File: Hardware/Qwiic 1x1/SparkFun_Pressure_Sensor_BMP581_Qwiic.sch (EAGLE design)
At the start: 25 parts, among them J1 QWIIC_RIGHT_ANGLE, J2 QWIIC_RIGHT_ANGLE, U1 BMP581

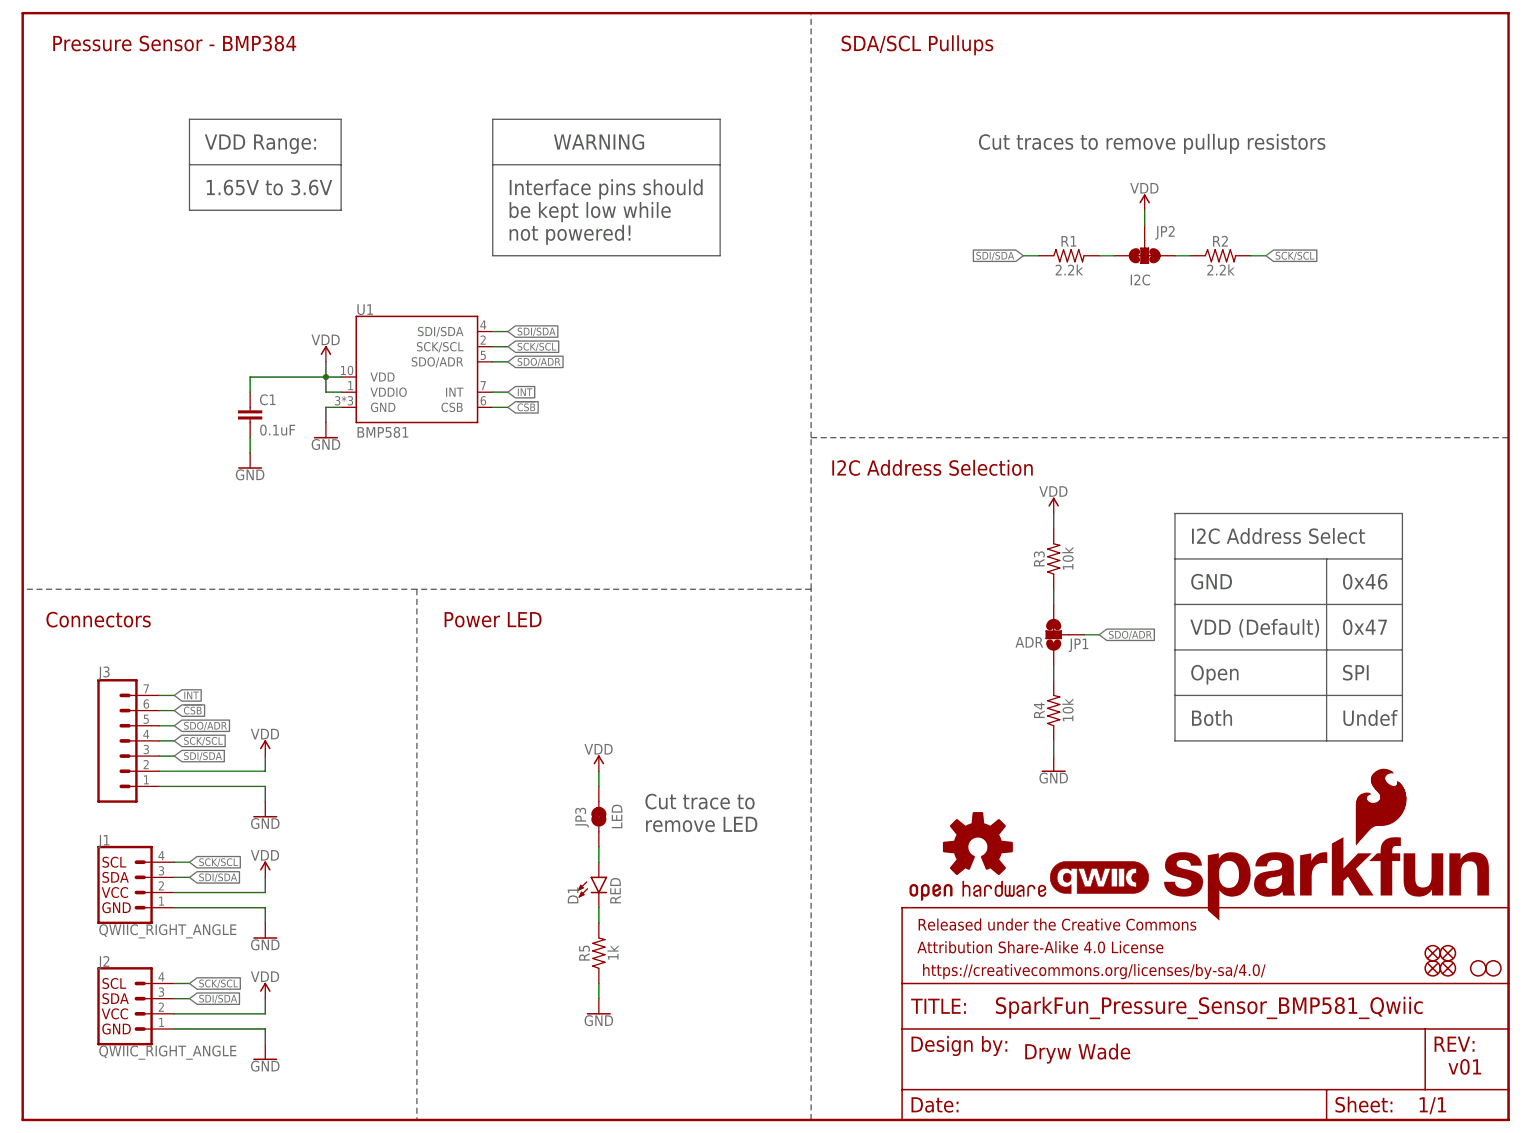
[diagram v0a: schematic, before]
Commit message: Design review updates
Rename files
Change to v10 (accelerating to reds)
Fix sensor name in schematic
Add note to schematic about max wire diameter in Micro PTH connectors
Update VDD range
Fix acid trap in Micro
Move PWR LED to give space
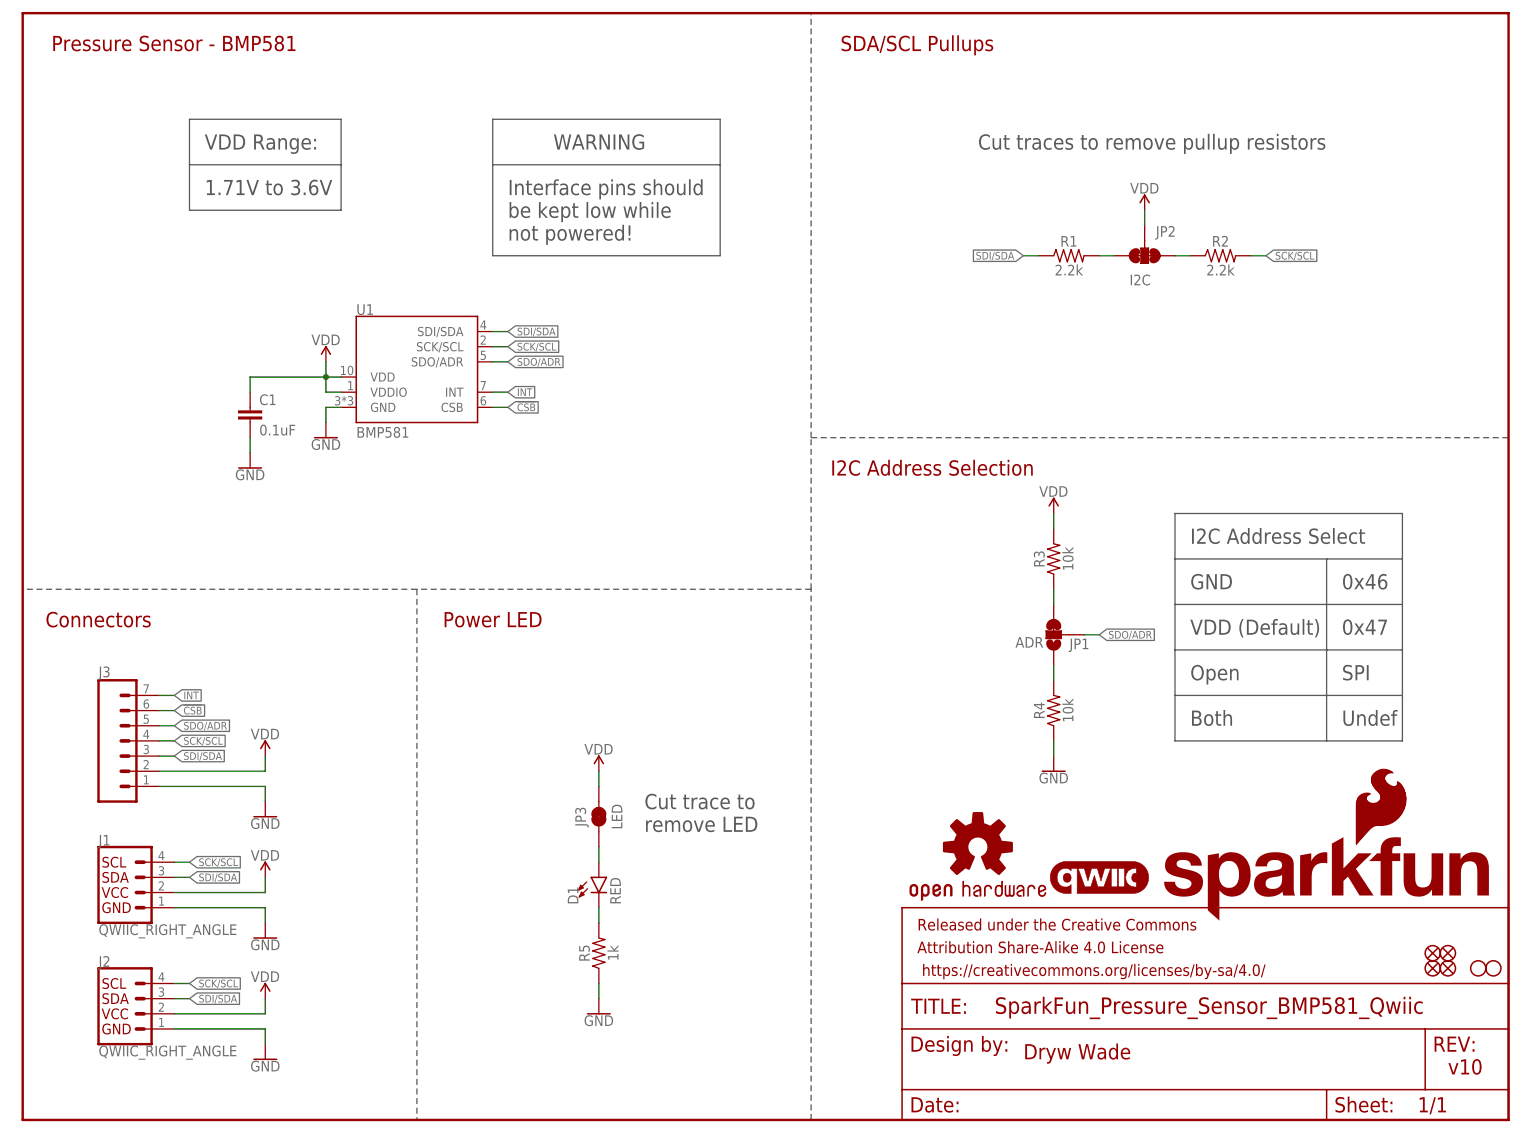
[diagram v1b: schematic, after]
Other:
- note added: "1.71V to 3.6V"
- note added: "Pressure Sensor - BMP581"
- note added: "v10"
- note removed: "1.65V to 3.6V"
- note removed: "Pressure Sensor - BMP384"
- note removed: "v01"
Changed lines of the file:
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@@
 <plain>
 <text x="167.64" y="10.16" size="2.54" layer="94" font="vector">Dryw Wade</text>
-<text x="238.76" y="7.62" size="2.54" layer="94" font="vector">v01</text>
+<text x="238.76" y="7.62" size="2.54" layer="94" font="vector">v10</text>
 <wire x1="132.08" y1="0" x2="132.08" y2="88.9" width="0.2032" layer="97" style="shortdash"/>
 <wire x1="132.08" y1="88.9" x2="132.08" y2="114.3" width="0.2032" layer="97" style="shortdash"/>
@@
 <wire x1="132.08" y1="88.9" x2="66.04" y2="88.9" width="0.2032" layer="97" style="shortdash"/>
 <text x="12.7" y="83.82" size="2.54" layer="94" font="vector" align="center">Connectors</text>
-<text x="25.4" y="180.34" size="2.54" layer="94" font="vector" align="center">Pressure Sensor - BMP384</text>
+<text x="25.4" y="180.34" size="2.54" layer="94" font="vector" align="center">Pressure Sensor - BMP581</text>
 <text x="152.4" y="109.22" size="2.54" layer="94" font="vector" align="center">I2C Address Selection</text>
 <text x="195.58" y="96.52" size="2.54" layer="97" font="vector">I2C Address Select</text>
@@
 <text x="160.02" y="162.56" size="2.54" layer="97" font="vector">Cut traces to remove pullup resistors</text>
 <text x="30.48" y="162.56" size="2.54" layer="97" font="vector">VDD Range:</text>
-<text x="30.48" y="154.94" size="2.54" layer="97" font="vector">1.65V to 3.6V</text>
+<text x="30.48" y="154.94" size="2.54" layer="97" font="vector">1.71V to 3.6V</text>
 <wire x1="27.94" y1="167.64" x2="27.94" y2="160.02" width="0.2032" layer="97"/>
 <wire x1="27.94" y1="160.02" x2="27.94" y2="152.4" width="0.2032" layer="97"/>
